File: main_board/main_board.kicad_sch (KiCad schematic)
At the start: 0 parts

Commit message: sch: update sch
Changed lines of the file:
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@@
 			)
 		)
-		(pin "I2C_SDA" input
-			(at 204.47 125.73 180)
+		(pin "BTN_BACK" input
+			(at 204.47 134.62 180)
 			(effects
 				(font
@@
 		)
 		(pin "I2C_SCL" input
-			(at 204.47 123.19 180)
+			(at 204.47 124.46 180)
+			(effects
+				(font
+					(size 1.27 1.27)
+				)
+				(justify left)
+			)
+		)
+		(pin "I2C_SDA" bidirectional
+			(at 204.47 127 180)
 			(effects
 				(font
@@
 		)
 		(pin "PERI_EN" input
-			(at 204.47 128.27 180)
+			(at 204.47 129.54 180)
 			(effects
 				(font
-					(size 1.27 1.27)
-				)
-				(justify left)
-			)
-		)
-		(pin "BTN_BACK" input
-			(at 204.47 134.62 180)
-			(effects
-				(font

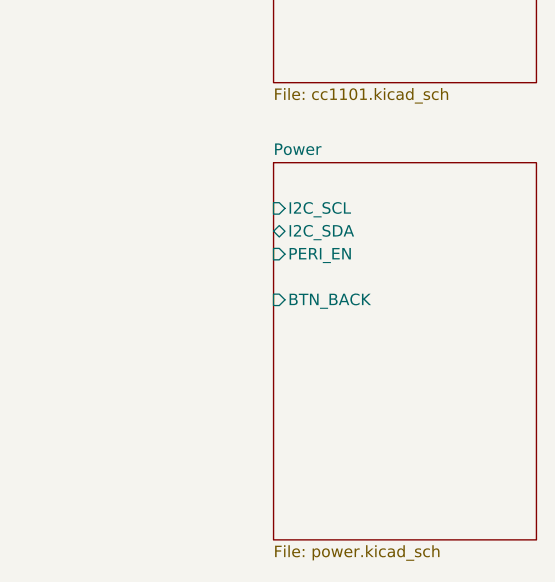
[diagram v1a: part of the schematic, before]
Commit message: sch: working on stm32wb55
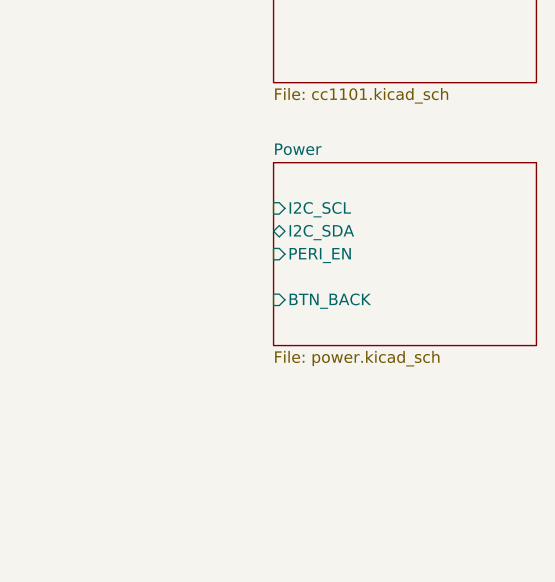
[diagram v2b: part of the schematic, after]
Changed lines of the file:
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@@
 	(sheet
 		(at 204.47 119.38)
-		(size 29.21 41.91)
+		(size 29.21 20.32)
 		(fields_autoplaced yes)
 		(stroke
@@
 		)
 		(property "Sheetfile" "power.kicad_sch"
-			(at 204.47 161.8746 0)
+			(at 204.47 140.2846 0)
 			(effects
 				(font
